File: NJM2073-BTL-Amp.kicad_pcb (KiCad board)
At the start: 2 copper layers, 18.2 x 3.5 mm, 86 parts, among them J1 Screw_Terminal_01x02, J2 Screw_Terminal_01x02, J3 Barrel_Jack_Switch, J4 Conn_Coaxial_x2, J5 AudioJack3_SwitchTR, U1 NJM2073, U2 NJM2073, U3 NJM4558, U4 NJM4558, U5 LM317_TO-220

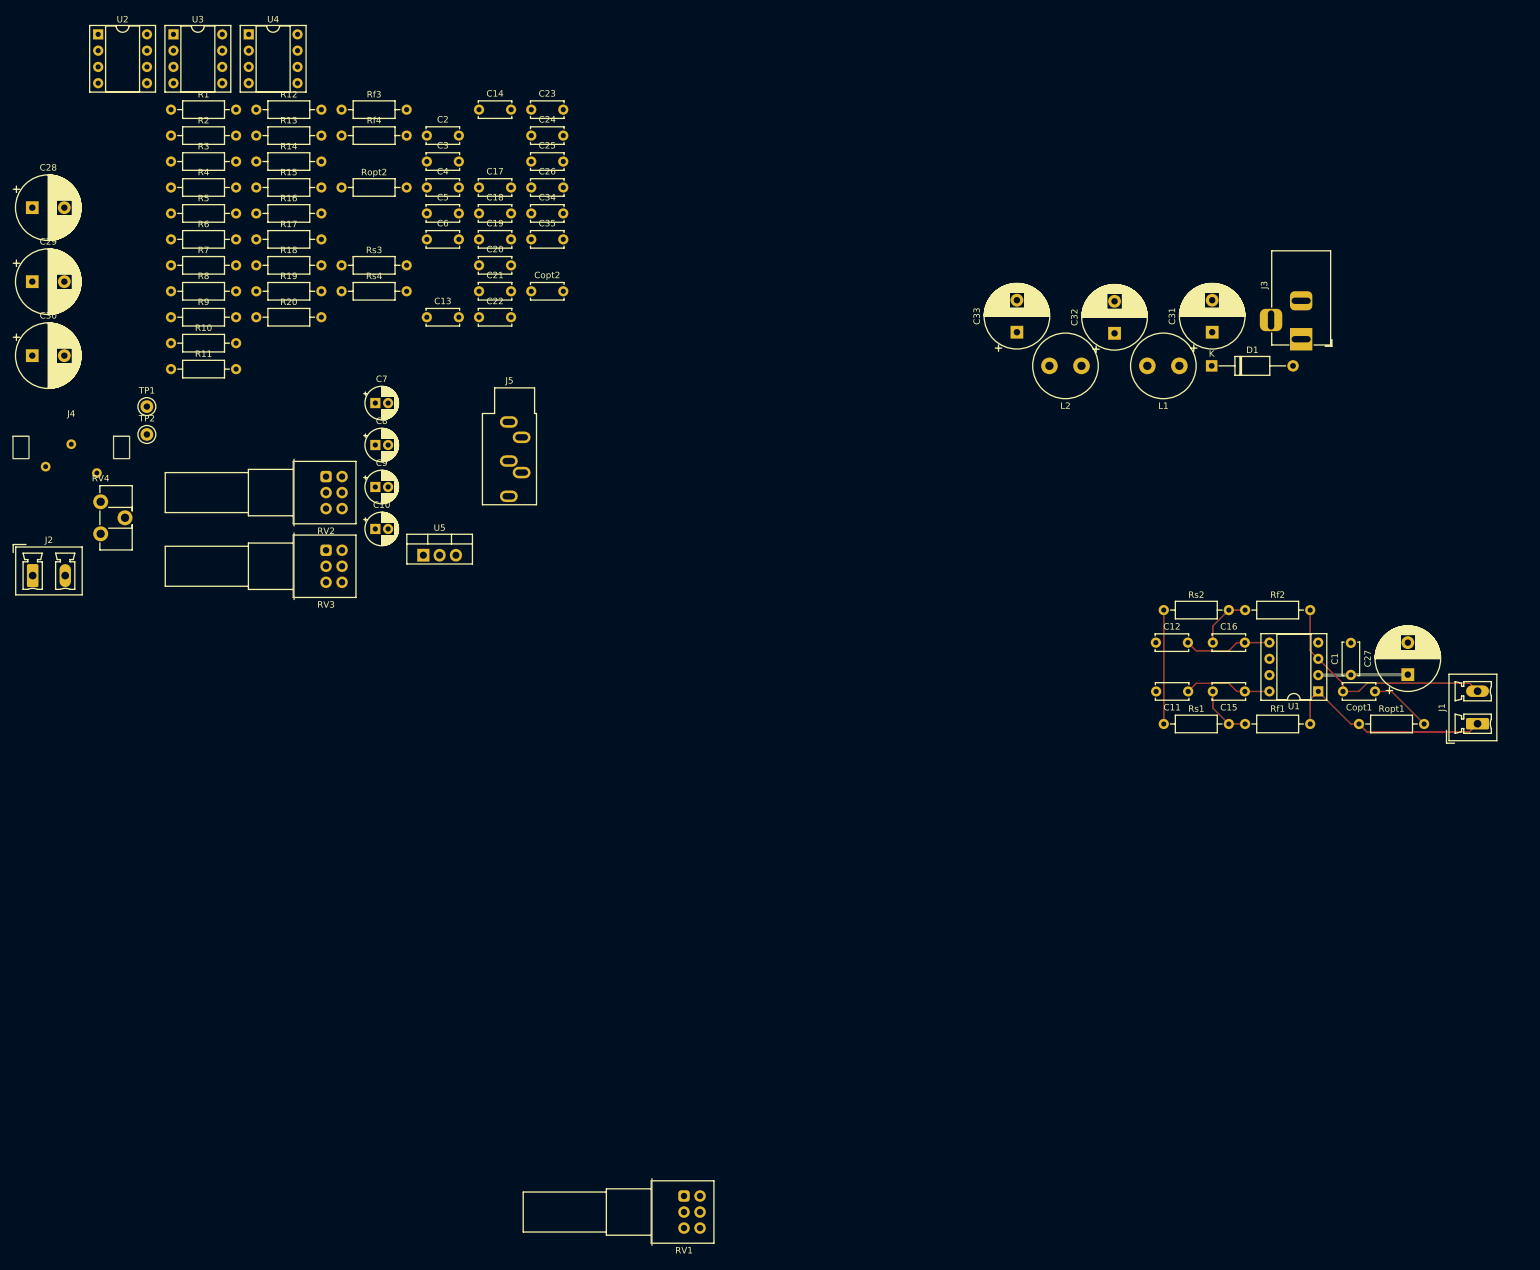
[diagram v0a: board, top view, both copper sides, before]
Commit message: BTL アンプ部構成・アンプ電源配置配線
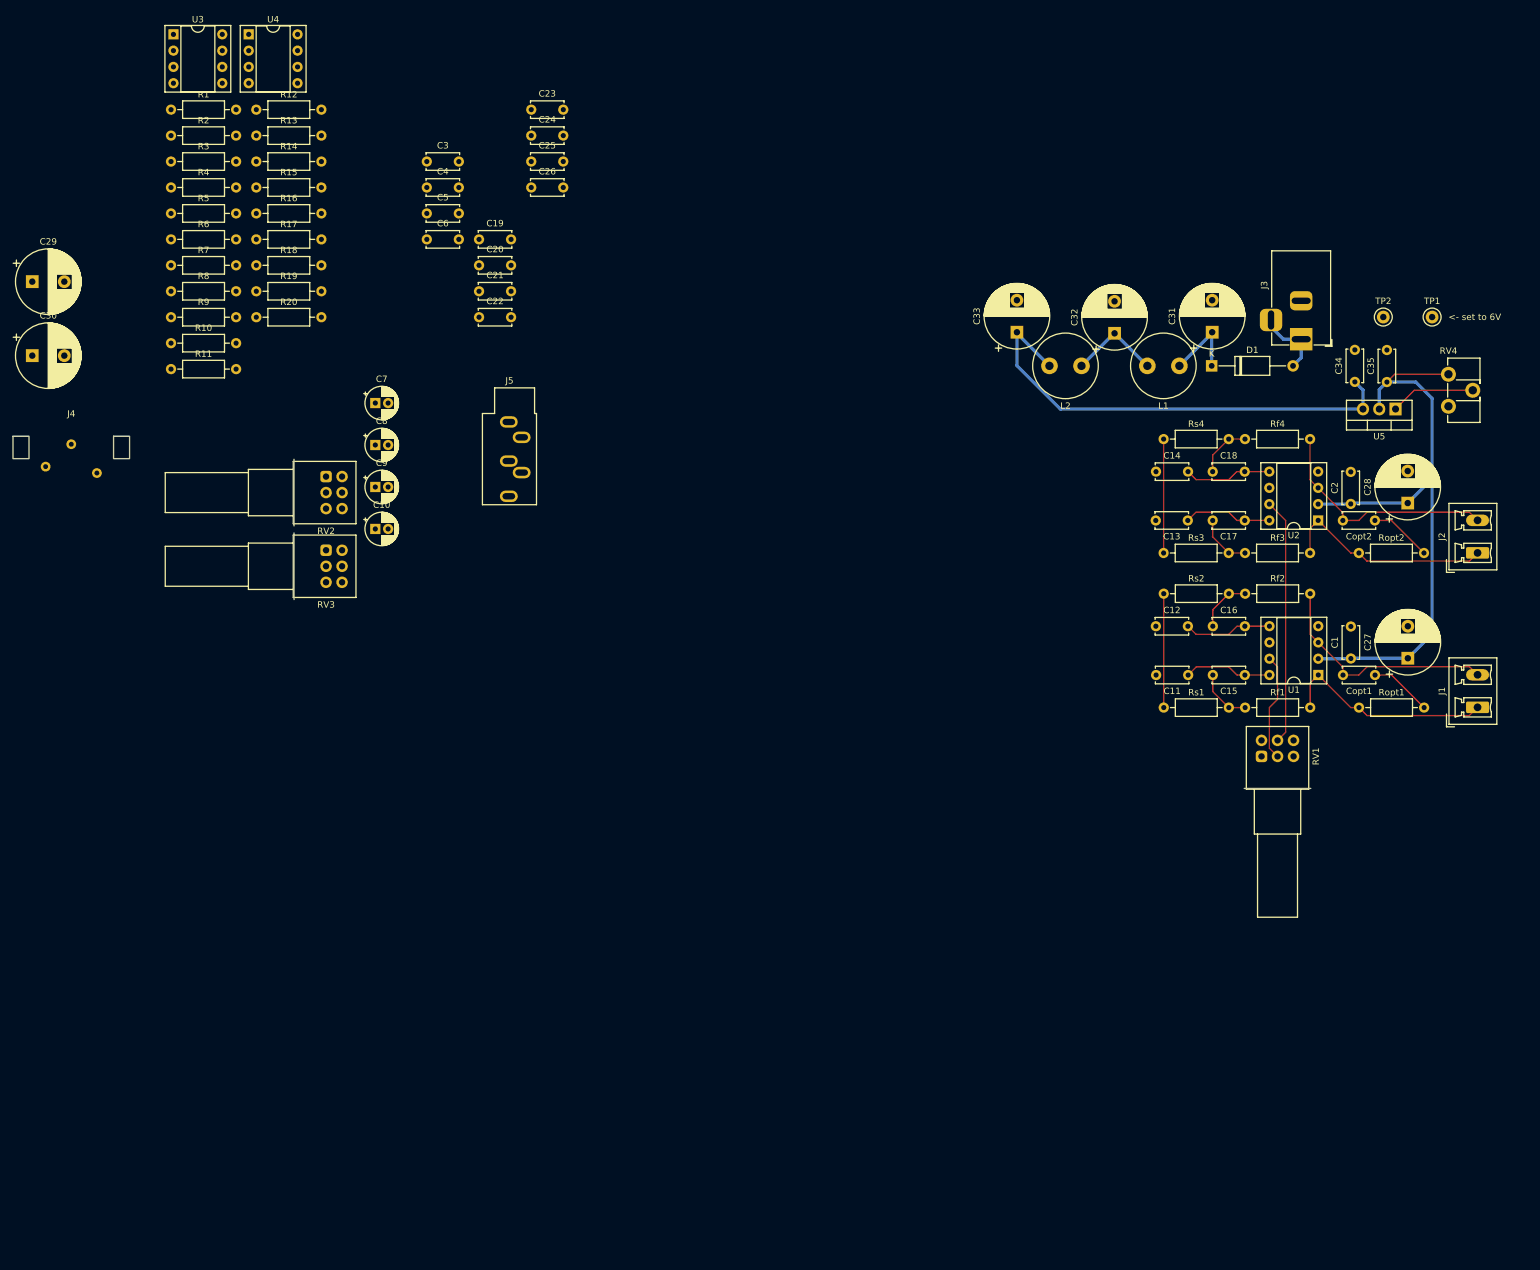
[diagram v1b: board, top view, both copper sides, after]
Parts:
- moved J2 225.6 mm to (242.0, 96.5), turned to 90 degrees
- moved C28 219.6 mm to (231.1, 88.7), turned to 90 degrees
- moved RV4 211.3 mm to (237.5, 68.6)
- moved U2 205.0 mm to (217.2, 91.4), turned to 180 degrees
- moved TP1 201.1 mm to (234.9, 59.7)
- moved TP2 193.9 mm to (227.3, 59.7)
- moved Ropt2 168.7 mm to (223.5, 96.5)
- moved Rf3 157.1 mm to (205.7, 96.5)
- moved C2 155.3 mm to (222.2, 88.9), turned to 90 degrees
- moved U5 153.5 mm to (229.2, 74.0), turned to 180 degrees
- moved Rf4 148.8 mm to (205.7, 78.7)
- moved Copt2 136.5 mm to (226.0, 91.4), turned to 180 degrees
- moved Rs3 136.0 mm to (193.0, 96.5)
- moved C35 135.4 mm to (227.9, 69.8), turned to 90 degrees
- moved C34 131.2 mm to (222.9, 69.8), turned to 90 degrees
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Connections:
- C14 pad 1: Net-(U2B-BIN-) -> GND
- C14 pad 2: GND -> Net-(U2B-BIN-)
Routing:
- net +6V: track 14.0 -> 98.4 mm
- net +12V: track 0.00 -> 74.3 mm
- net Net-(U2A-AIN+): track 0.00 -> 38.5 mm
- net Net-(J2-Pin_2): track 0.00 -> 36.9 mm
- net Net-(J2-Pin_1): track 0.00 -> 33.6 mm
- net Net-(Rs3-Pad1): track 0.00 -> 17.8 mm
- net Net-(U1A-AIN+): track 0.00 -> 16.8 mm
- net Net-(C32-Pad1): track 0.00 -> 14.5 mm
- net Net-(U2A-AIN-): track 0.00 -> 13.8 mm
- net Net-(U2B-BIN-): track 0.00 -> 13.7 mm
- net Net-(U5-ADJ): track 0.00 -> 13.3 mm
- net Net-(D1-K): track 0.00 -> 12.7 mm
- net VCC: track 0.00 -> 11.3 mm
- net Net-(Copt2-Pad1): track 0.00 -> 9.79 mm
- net Net-(C17-Pad2): track 0.00 -> 8.69 mm
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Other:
- board text added: "<- set to 6V"

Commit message: 基板作成
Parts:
- removed R5, R6: 100k, Resistor_THT:R_Axial_DIN0207_L6.3mm_D2.5mm_P10.16mm_Horizontal
- moved U3 158.0 mm to (170.2, 102.9), turned to 180 degrees
- moved R8 155.6 mm to (184.2, 109.2), turned to -90 degrees
- moved R10 149.4 mm to (184.2, 95.2), turned to 90 degrees
- moved R7 147.6 mm to (174.0, 109.2), turned to -90 degrees
- moved R17 145.0 mm to (185.5, 102.9), turned to 180 degrees
- moved R9 138.3 mm to (174.0, 85.1), turned to -90 degrees
- moved R19 136.0 mm to (185.5, 78.7), turned to 180 degrees
- moved U4 135.6 mm to (170.2, 78.7), turned to 180 degrees
- moved R18 133.1 mm to (175.3, 100.3)
- moved R11 131.2 mm to (158.8, 119.4), turned to 90 degrees
- moved R12 130.3 mm to (143.6, 119.4), turned to 90 degrees
- moved C29 127.6 mm to (133.3, 105.4), turned to 180 degrees
- moved R13 127.3 mm to (151.2, 110.5), turned to 90 degrees
- moved R20 125.0 mm to (175.3, 76.2)
- moved R14 122.9 mm to (158.8, 95.2), turned to 90 degrees
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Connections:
- C3 pad 1: +12V -> GND
- C3 pad 2: GND -> +12V
- C4 pad 1: +12V -> GND
- C4 pad 2: GND -> +12V
- R11 pad 1: Net-(C7-Pad2) -> Net-(C20-Pad1)
- R11 pad 2: Net-(C20-Pad1) -> Net-(C7-Pad2)
- R14 pad 1: Net-(C9-Pad2) -> Net-(C24-Pad1)
- R14 pad 2: Net-(C24-Pad1) -> Net-(C9-Pad2)
- R18 pad 1: Net-(C19-Pad2) -> Net-(U3A--)
- R18 pad 2: Net-(U3A--) -> Net-(C19-Pad2)
- R20 pad 1: Net-(C23-Pad2) -> Net-(U4A--)
- R20 pad 2: Net-(U4A--) -> Net-(C23-Pad2)
- R8 pad 1: Net-(R8-Pad1) -> Net-(C8-Pad1)
- R8 pad 2: Net-(C8-Pad1) -> Net-(R8-Pad2)
- RV2 pad 1: Net-(R8-Pad1) -> Net-(R8-Pad2)
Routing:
- net +12V: track 74.3 -> 240.3 mm
- net Net-(C23-Pad2): track 0.00 -> 74.5 mm
- net Net-(C8-Pad1): track 0.00 -> 58.0 mm
- net Net-(C24-Pad2): track 0.00 -> 57.9 mm, vias 0 -> 1
- net Net-(C10-Pad1): track 0.00 -> 57.9 mm
- net Net-(R10-Pad1): track 0.00 -> 53.6 mm
- net Net-(C19-Pad2): track 0.00 -> 52.9 mm, vias 0 -> 1
- net Filtered-signal-R: track 0.00 -> 52.5 mm
- net Net-(U3A-+): track 0.00 -> 44.7 mm
- net Net-(U4A-+): track 0.00 -> 44.6 mm
- net Net-(R9-Pad2): track 0.00 -> 44.6 mm
- net Net-(U3B--): track 0.00 -> 40.3 mm
- net Net-(U4B--): track 0.00 -> 40.3 mm
- net Net-(C24-Pad1): track 0.00 -> 39.7 mm
- net Net-(C25-Pad1): track 0.00 -> 39.6 mm
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- added copper zone on B.Cu, net GND
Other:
- board size 18.2 x 3.5 mm -> 133.4 x 80.6 mm
- board text added: "NJM2073D Stereo BTL Speaker AMP MOS@53175DDD / MOS Electronics"

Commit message: ちょっと修正
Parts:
- moved R18 3.77 mm to (179.1, 100.3)
- moved R20 3.77 mm to (179.1, 76.2)
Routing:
- net GND: track 15.2 -> 27.9 mm, vias 24 -> 34
- net Net-(C19-Pad2): track 52.9 -> 48.8 mm, vias 1 -> 0
- net Net-(C23-Pad2): track 74.5 -> 75.0 mm

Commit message: シルク印刷追加
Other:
- board text added: "v0.1"
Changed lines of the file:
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@@
 			(outputformat 1)
 			(mirror no)
-			(drillshape 1)
+			(drillshape 0)
 			(scaleselection 1)
-			(outputdirectory "")
+			(outputdirectory "PCB/")
 		)
 	)
@@
 		(layer "F.SilkS")
 		(effects
+			(font
+				(size 1.5 1.5)
+				(thickness 0.1875)
+			)
+			(justify left)
+		)
+	)
+	(gr_text "v0.1"
+		(at 226.06 130.81 0)
+		(layer "F.SilkS")
+		(effects

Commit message: 抵抗値修正
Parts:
- Rf1, Rf2, Rf3, Rf4: value 5k -> 4.7k
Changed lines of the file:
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@@
 			)
 		)
-		(property "Value" "5k"
+		(property "Value" "4.7k"
 			(at 5.08 2.37 0)
 			(layer "F.Fab")
@@
 			)
 		)
-		(property "Value" "5k"
+		(property "Value" "4.7k"
 			(at 5.08 2.37 0)
 			(layer "F.Fab")
@@
 			)
 		)
-		(property "Value" "5k"
+		(property "Value" "4.7k"
 			(at 5.08 2.37 0)
 			(layer "F.Fab")
@@
 			)
 		)
-		(property "Value" "5k"
+		(property "Value" "4.7k"
 			(at 5.08 2.37 0)
 			(layer "F.Fab")
